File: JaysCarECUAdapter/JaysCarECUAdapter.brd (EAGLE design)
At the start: 64.4 x 33 mm, 2 parts

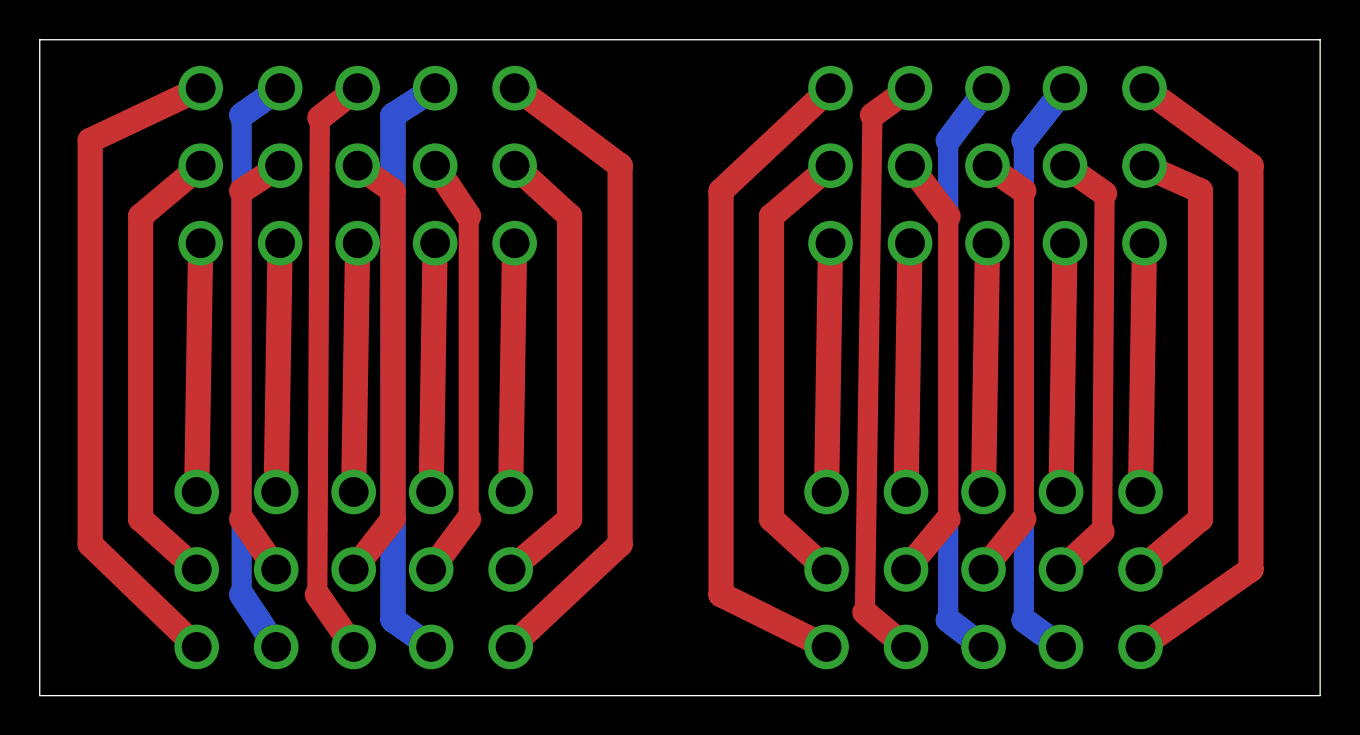
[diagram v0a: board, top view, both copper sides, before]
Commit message: Increased trace thickness.
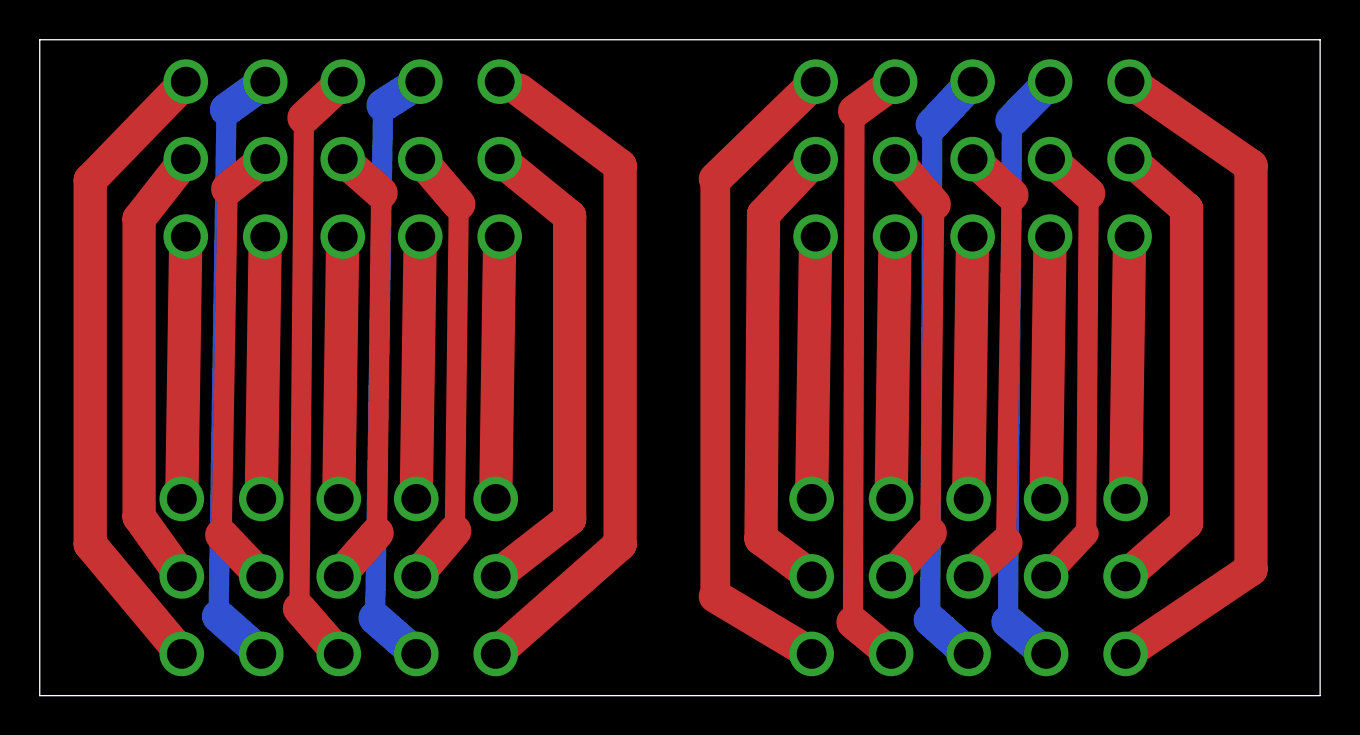
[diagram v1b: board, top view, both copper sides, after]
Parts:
- moved U$2 0.83 mm to (31.0, 6.00)
- moved U$1 0.82 mm to (31.0, 27.0)
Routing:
- net N$26: track 33.7 -> 35.4 mm
- net N$12: track 33.2 -> 34.8 mm
- net N$10: track 22.9 -> 24.5 mm
- net N$30: track 33.9 -> 32.4 mm
- net N$2: track 29.7 -> 30.8 mm
- net N$7: track 21.5 -> 22.4 mm
- net N$20: track 29.7 -> 30.5 mm
- net N$1: track 21.9 -> 22.7 mm
- net N$5: track 29.6 -> 30.4 mm
- net N$16: track 21.7 -> 22.5 mm
- net N$19: track 22.0 -> 22.7 mm
- net N$24: track 29.8 -> 30.5 mm
- net N$4: track 21.9 -> 22.6 mm
- net N$18: track 30.1 -> 30.7 mm
- net N$8: track 12.5 -> 13.2 mm
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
